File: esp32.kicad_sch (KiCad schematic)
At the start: 43 parts, among them IC3 ESP32-C3, IC4 W25Q32RVXHJQ_TR, IC5 NJM2882F33-TE1, IC6 CP2102-GM, Q1 SS8050-G, Q2 SS8050-G, Y1 CM7V-T1A-32.768KHZ-7PF-20PPM-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, Y2 ABM8-40.000MHZ-10-1-U-T

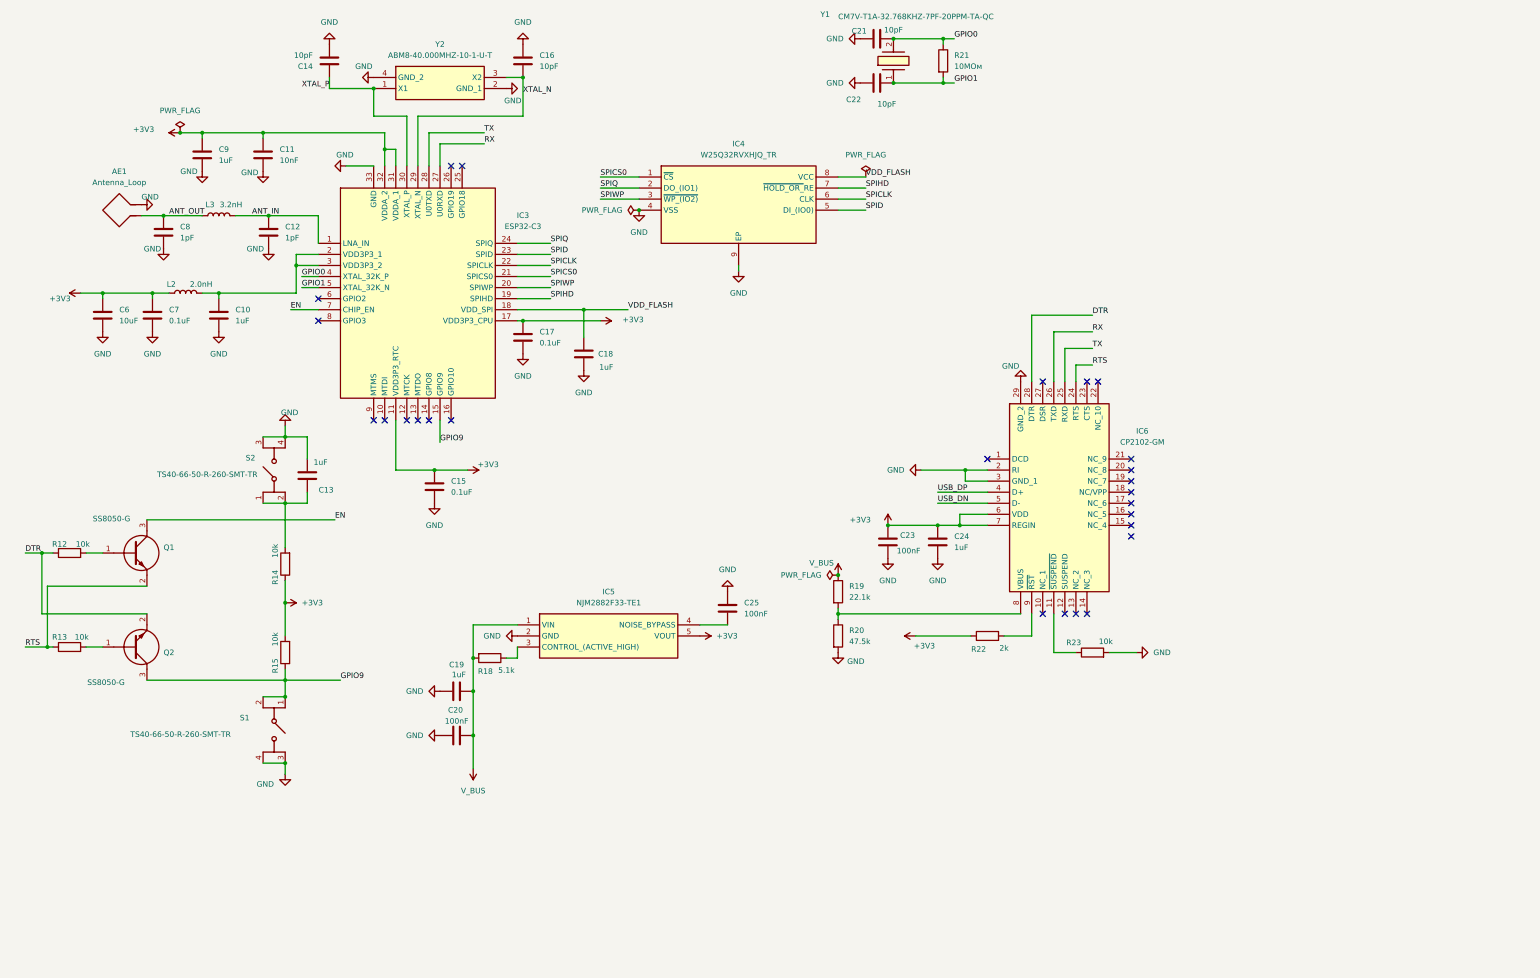
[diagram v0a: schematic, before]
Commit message: improve power delivery schema, improve dac, added oled, encoder, audio out
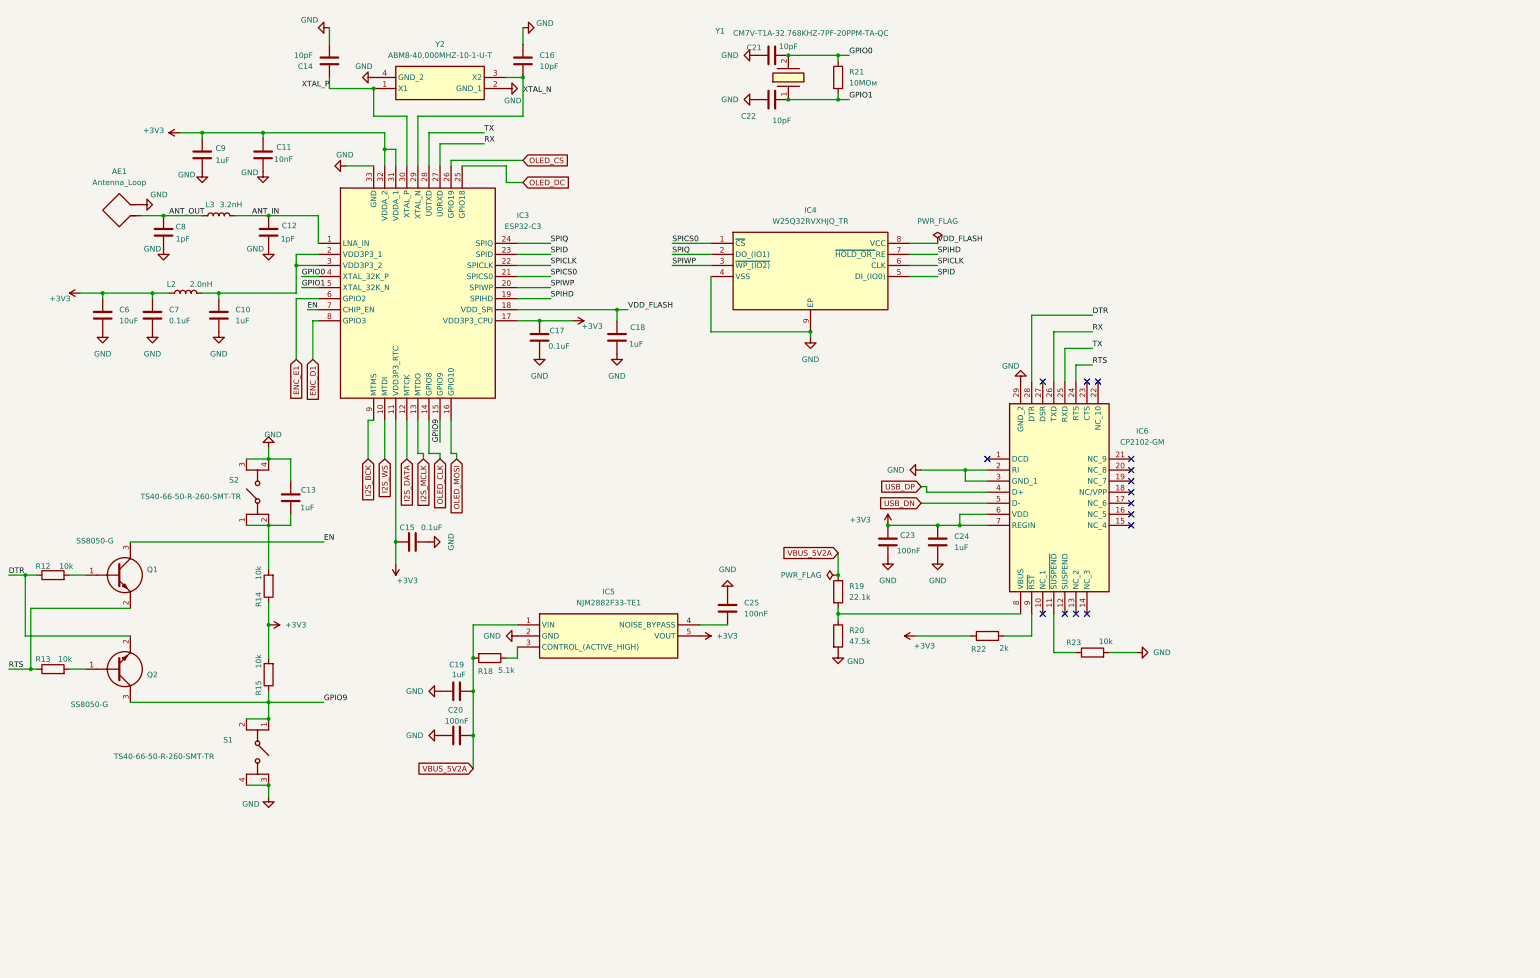
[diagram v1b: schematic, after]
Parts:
- AE1: footprint esp32_selfmade:2.4_antenna_TI -> ipradio:2.4_antenna_TI
- IC3: footprint QFN50P500X500X90-33N-D -> ipradio:QFN50P500X500X90-33N-D
- IC4: footprint SON50P300X200X40-9N -> ipradio:SON50P300X200X40-9N
- IC5: footprint esp32_selfmade:SOT95P280X130-5N -> ipradio:SOT95P280X130-5N
- IC6: footprint QFN50P500X500X100-29N-D -> ipradio:QFN50P500X500X100-29N-D
- Q1, Q2: footprint SOT95P240X115-3N -> ipradio:SOT95P240X115-3N
- S1, S2: footprint TS406650R260SMTTR -> ipradio:TS406650R260SMTTR
- Y1: footprint CM7V32768TBQA020 -> ipradio:CM7V32768TBQA020
- Y2: footprint ABM810000MHZ12D2W -> ipradio:ABM810000MHZ12D2W
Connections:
- net I2S_WS: now reaches IC3.10 (MTDI)
- net I2S_DATA: now reaches IC3.12 (MTCK)
- net I2S_MCLK: now reaches IC3.13 (MTDO)
- net OLED_CLK: now reaches IC3.14 (GPIO8)
- net OLED_MOSI: now reaches IC3.16 (GPIO10)
- net OLED_DC: now reaches IC3.25 (GPIO18)
- net OLED_CS: now reaches IC3.26 (GPIO19)
- net ENC_E1: now reaches IC3.6 (GPIO2)
- net ENC_D1: now reaches IC3.8 (GPIO3)
- net I2S_BCK: now reaches IC3.9 (MTMS)
- net V_BUS renamed VBUS_5V2A
- no-connect marks 26 -> 15
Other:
- moved on the sheet: C13, C17, C18, C21, C22, IC4, Q1, Q2, R12, R13, R14, R15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

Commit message: finalize power and esp schemas
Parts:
- removed C19: 1uF, Capacitor_SMD:C_0402_1005Metric, symbol Device:C
- removed C20, C25: 100nF, Capacitor_SMD:C_0402_1005Metric, symbol Device:C
- removed IC5: NJM2882F33-TE1, ipradio:SOT95P280X130-5N, symbol esp32_selfmade_Esp_32_module:NJM2882F33-TE1
- removed R18: 5.1k, Resistor_SMD:R_0402_1005Metric, symbol Device:R
- added C1, C2: 1uF, Capacitor_SMD:C_0402_1005Metric, symbol Device:C
- added IC1: AP2112K-3.3TRG1, ipradio:SOT95P285X140-5N, symbol ipradio:AP2112K-3.3TRG1
- added R24: 100k, Resistor_SMD:R_0402_1005Metric, symbol Device:R
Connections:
- net +3V3: now also C2.1, IC1.5 (VOUT)
- net GND: now also C1.2, C2.2, IC1.2 (GND)
- net VBUS_5V2A renamed +5V_BUS
- net +5V_BUS: now also C1.1, IC1.1 (VIN), R24.2
- new net: IC1.3 (EN), R24.1
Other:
- moved on the sheet: IC4

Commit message: finalized schema
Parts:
- removed AE1: Antenna_Loop, ipradio:2.4_antenna_TI, symbol Device:Antenna_Loop
- removed C1, C2: 1uF, Capacitor_SMD:C_0402_1005Metric, symbol Device:C
- removed IC1: AP2112K-3.3TRG1, ipradio:SOT95P285X140-5N, symbol ipradio:AP2112K-3.3TRG1
- removed R24: 100k, Resistor_SMD:R_0402_1005Metric, symbol Device:R
- added 3C19, 4C18: 100nF, Capacitor_SMD:C_0402_1005Metric, symbol Device:C
- added 3C20, 4C17, C19, C20: 1uF, Capacitor_SMD:C_0402_1005Metric, symbol Device:C
- added 3C21: 10uF, Capacitor_SMD:C_0402_1005Metric, symbol Device:C
- added 3FB1: 100mHz, Inductor_SMD:L_0402_1005Metric, symbol Device:FerriteBead
- added IC10: SPX1117M3-L-3-3_TR, ipradio:SOT230P700X180-4N, symbol ipradio:SPX1117M3-L-3-3_TR
- added J4: CONMHF1-SMD-T, ipradio:CONMHF1SMDT, symbol ipradio:CONMHF1-SMD-T
- added R1: 10k, Resistor_SMD:R_0402_1005Metric, symbol Device:R
- added U2: SMS-202C, ipradio:SMS202F, symbol ipradio:SMS-202C
- C15, C17: value 0.1uF -> 100nF
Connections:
- net +3V3: now also 4C17.1, 4C18.1, C19.1, C20.1, IC10.2 (VOUT_1), IC10.4 (VOUT_2), R1.1
- net ANT_OUT: now also J4.1 (SIGNAL)
- net EN: now also C13.1, R14.2, S2.1 (COM_1), S2.2 (COM_2)
- net GND: now also C16.2, S1.1 (COM_1), S1.2 (COM_2), 3C19.2, 3C20.2, 3C21.2, 4C17.2, 4C18.2, C19.2, C20.2, IC10.1 (ADJ/GND), J4.2 (GND_1), J4.3 (GND_2), J4.4 (GND_3), U2.1, U2.10, U2.11, U2.12, U2.2, U2.3, U2.4, U2.5, U2.6, U2.7, U2.8, U2.9; no longer C16.1, IC6.2 (RI), S1.3 (NO_1), S1.4 (NO_2)
- net GPIO9: now also S1.3 (NO_1), S1.4 (NO_2); no longer S1.1 (COM_1), S1.2 (COM_2)
- net XTAL_N: now also C16.1; no longer C16.2
- net +5V_BUS renamed V_SYS_5V2A
- net V_SYS_5V2A: now also 3FB1.2
- net ENC_D1 renamed GPIO3
- net ENC_E1 renamed ENC_SW
- net I2S_MCLK renamed I2S_CLK
- net OLED_CLK renamed GPIO8
- net GPIO8: now also R1.2
- net OLED_CS renamed ENC_CLK
- net OLED_DC renamed ENC_DT
- net OLED_MOSI renamed I2S_SDA
- new net: 3C19.1, 3C20.1, 3C21.1, 3FB1.1, IC10.3 (VIN)
- no-connect marks 15 -> 16
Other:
- moved on the sheet: C10, C11, C12, C13, C14, C15, C16, C17, C18, C21, C22, C23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

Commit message: pcb for power and esp32
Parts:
- removed C21, C22: 10pF, Capacitor_SMD:C_0402_1005Metric, symbol Device:C
- removed R21: 10МОм, Resistor_SMD:R_0402_1005Metric, symbol Device:R
- removed Y1: CM7V-T1A-32.768KHZ-7PF-20PPM-TA-QC, ipradio:CM7V32768TBQA020, symbol ipradio:CM7V-T1A-32.768KHZ-7PF-20PPM-TA-QC
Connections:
- net GPIO3 is gone; now on net ENC_CLK: IC3.8 (GPIO3)
- net ENC_CLK: no longer IC3.26 (GPIO19)
- new net GPIO19: IC3.26 (GPIO19)
- no-connect marks 16 -> 19
